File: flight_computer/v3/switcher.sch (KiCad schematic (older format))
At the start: 56 parts, among them J10 Perovskite 3, J11 GaAs Panel, J12 GaAs Temperature, J13 Perovskite 1, J14 Perovskite 2, U15 74HC237, U2 CD4518BM96, U4 74HC237, U42 ADG839YKSZ-REEL7, U43 ADG839YKSZ-REEL7, U44 ADG839YKSZ-REEL7, U45 ADG839YKSZ-REEL7, U46 ADG839YKSZ-REEL7, U47 ADG839YKSZ-REEL7, U48 ADG839YKSZ-REEL7, U49 ADG839YKSZ-REEL7, U5 74HC237, U50 ADG839YKSZ-REEL7, U51 ADG839YKSZ-REEL7, U52 ADG839YKSZ-REEL7, U53 ADG839YKSZ-REEL7, U54 ADG839YKSZ-REEL7, U55 ADG839YKSZ-REEL7, U56 ADG839YKSZ-REEL7, U57 ADG839YKSZ-REEL7, U58 ADG839YKSZ-REEL7, U59 ADG839YKSZ-REEL7, U6 4012

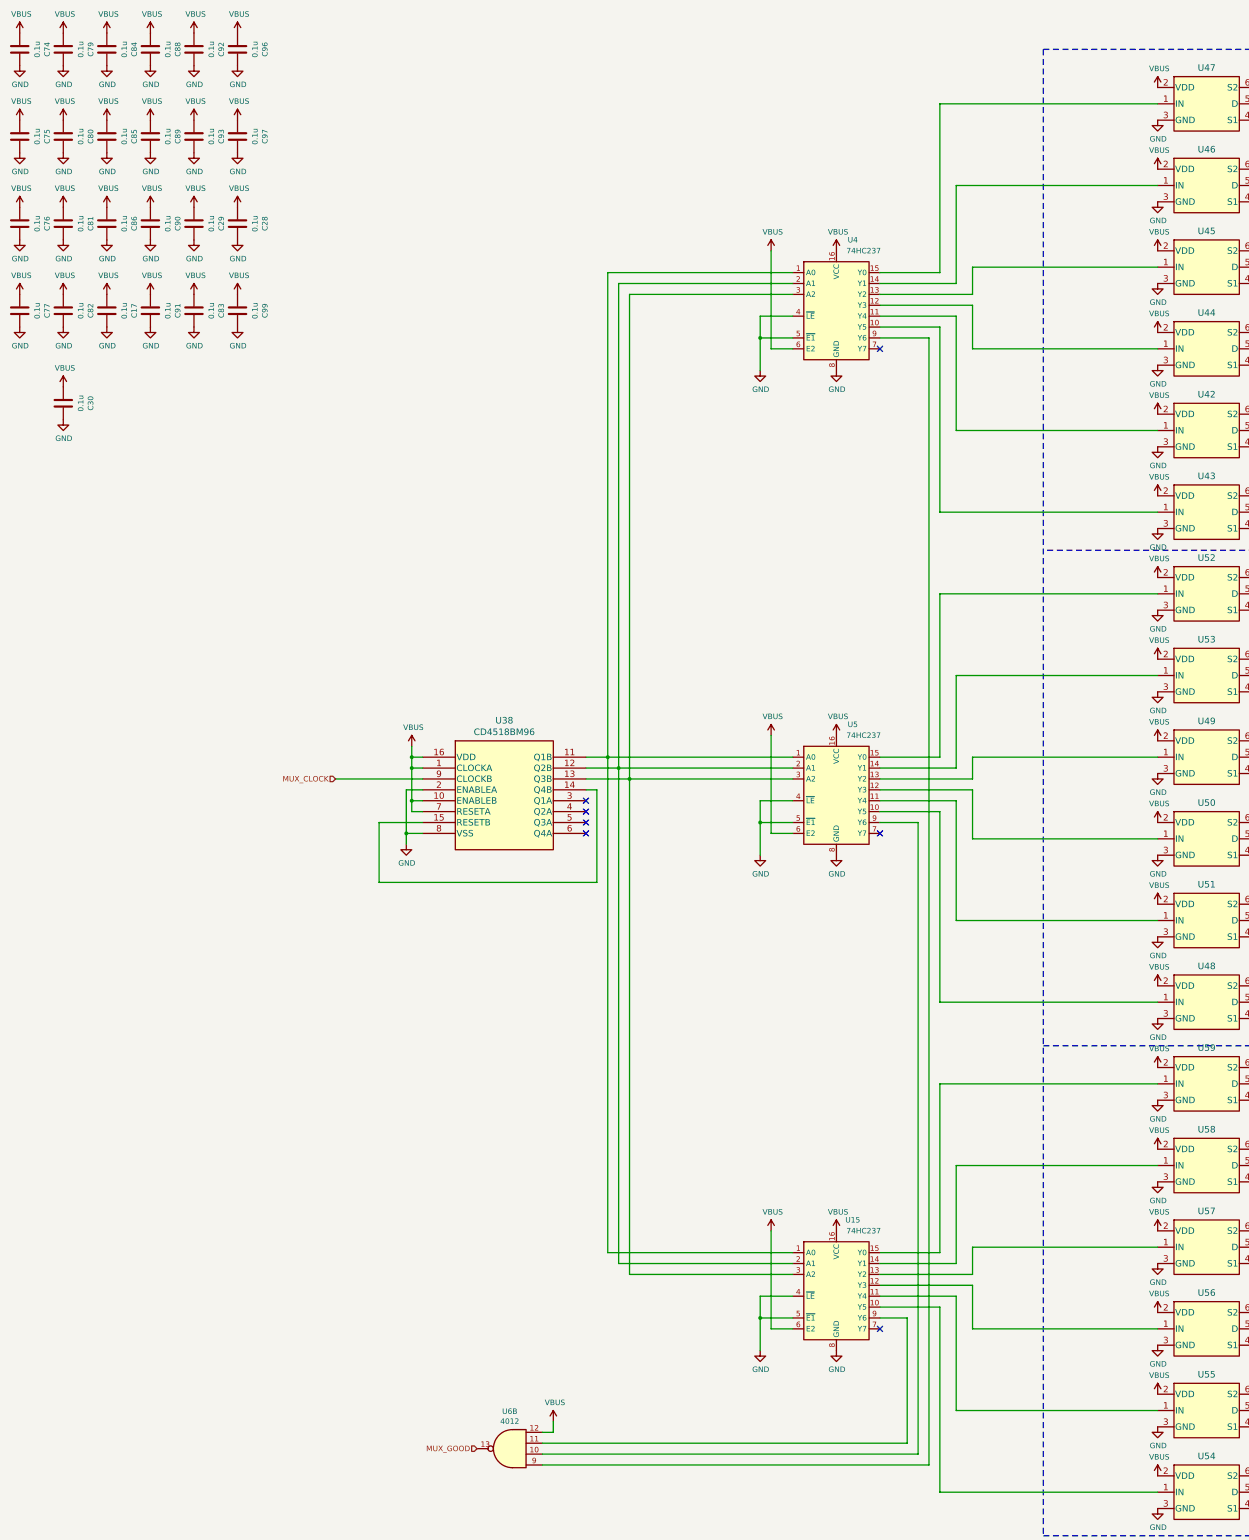
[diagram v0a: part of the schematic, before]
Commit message: Updating based on harnesses
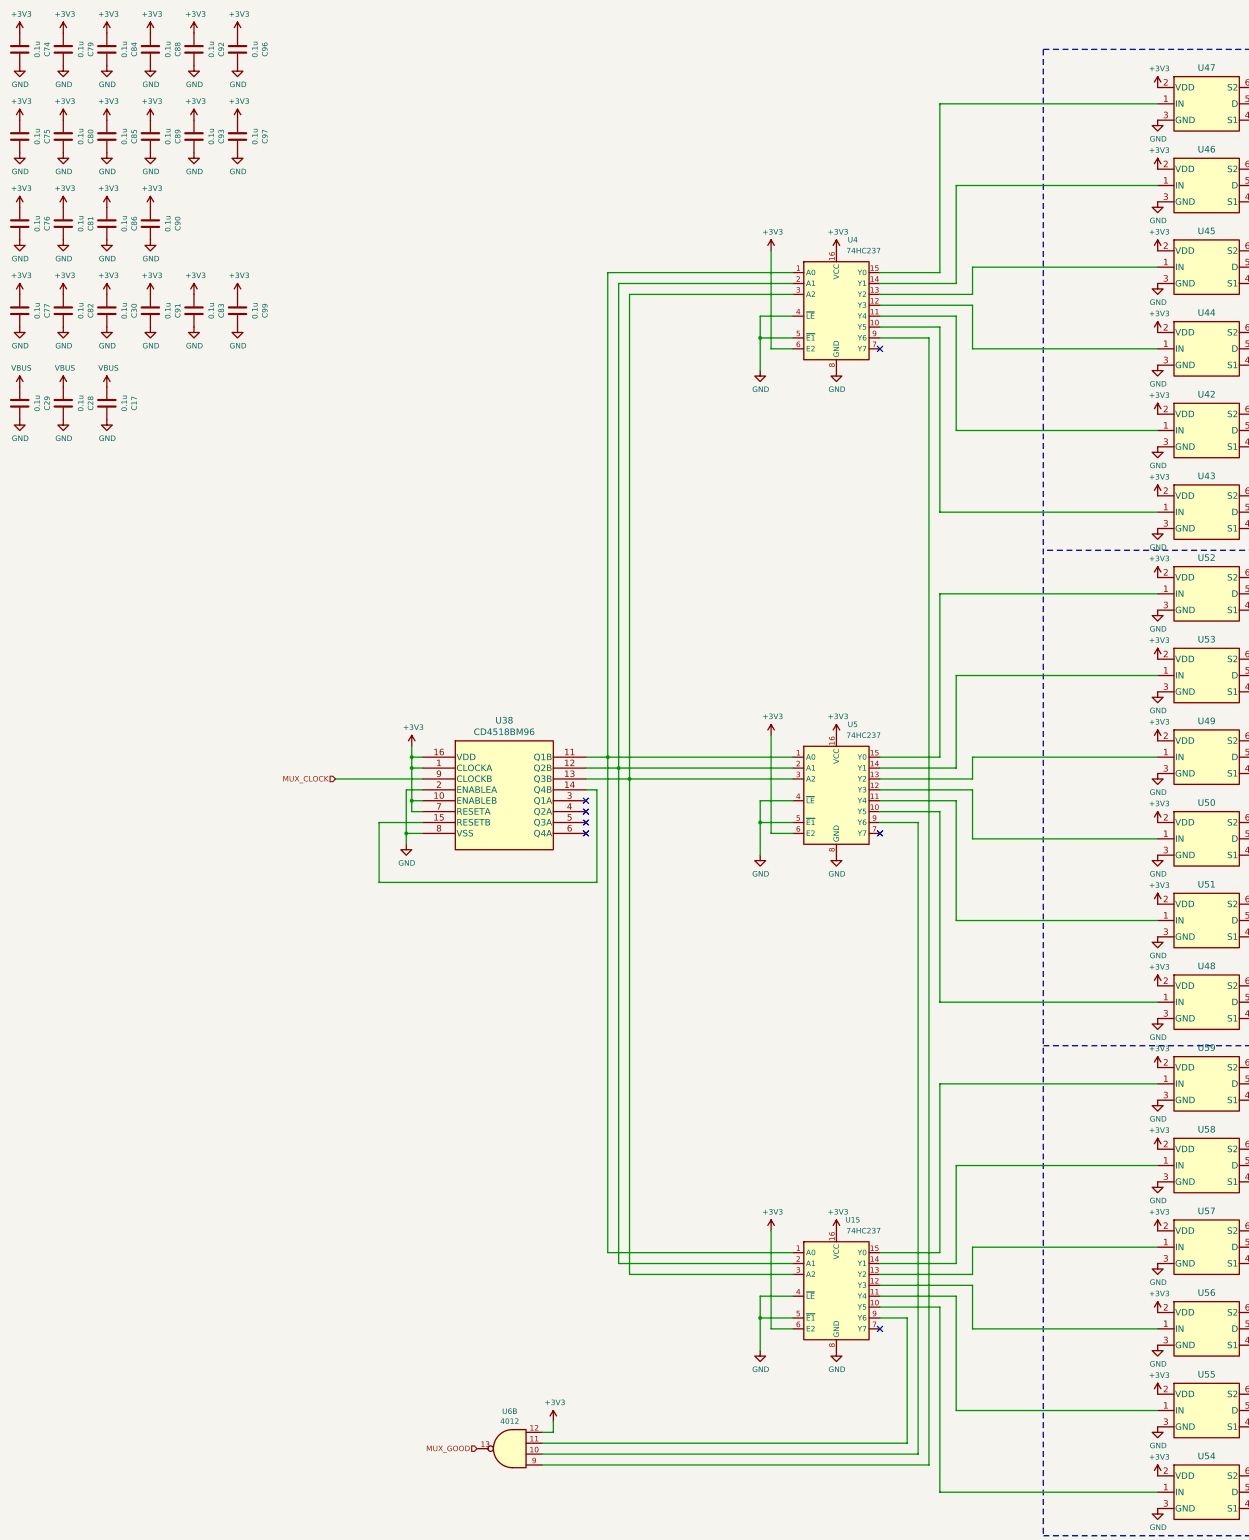
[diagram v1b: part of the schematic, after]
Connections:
- net VBUS: no longer C10.1, C14.1, C16.1, C18.1, C20.1, C25.1, C30.1, C4.1, C6.1, C75.1, C76.1, C8.1, C80.1, C81.1, C83.1, C85.1, C86.1, C89.1, C90.1, C93.1, C97.1, C99.1, U15.16 (VCC), U15.6 (E2), U2.1 (CLOCKA), U2.10 (ENABLEB), U2.16 (VDD), U2.7 (RESETA), U4.16 (VCC), U4.6 (E2), U42.2 (VDD), U43.2 (VDD), U44.2 (VDD), U45.2 (VDD), U46.2 (VDD), U47.2 (VDD), U48.2 (VDD), U49.2 (VDD), U5.16 (VCC), U5.6 (E2), U50.2 (VDD), U51.2 (VDD), U52.2 (VDD), U53.2 (VDD), U54.2 (VDD), U55.2 (VDD), U56.2 (VDD), U57.2 (VDD), U58.2 (VDD), U59.2 (VDD), U6.12
- new net +3V3: C10.1, C14.1, C16.1, C18.1, C20.1, C25.1, C30.1, C4.1, C6.1, C75.1, C76.1, C8.1, C80.1, C81.1, C83.1, C85.1, C86.1, C89.1, C90.1, C93.1, C97.1, C99.1, U15.16 (VCC), U15.6 (E2), U2.1 (CLOCKA), U2.10 (ENABLEB), U2.16 (VDD), U2.7 (RESETA), U4.16 (VCC), U4.6 (E2), U42.2 (VDD), U43.2 (VDD), U44.2 (VDD), U45.2 (VDD), U46.2 (VDD), U47.2 (VDD), U48.2 (VDD), U49.2 (VDD), U5.16 (VCC), U5.6 (E2), U50.2 (VDD), U51.2 (VDD), U52.2 (VDD), U53.2 (VDD), U54.2 (VDD), U55.2 (VDD), U56.2 (VDD), U57.2 (VDD), U58.2 (VDD), U59.2 (VDD), U6.12
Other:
- moved on the sheet: C17, C28, C29, C30

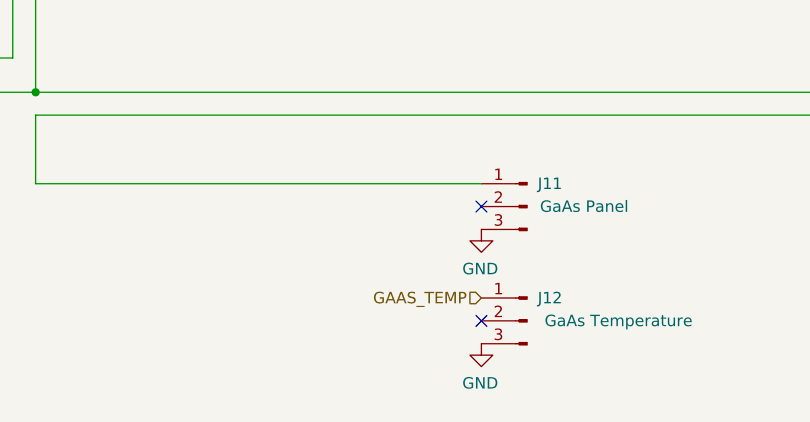
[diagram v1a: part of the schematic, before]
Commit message: Integrating flight computer
- EPS commands tested and working
- Updated v3, fixing connector polarity
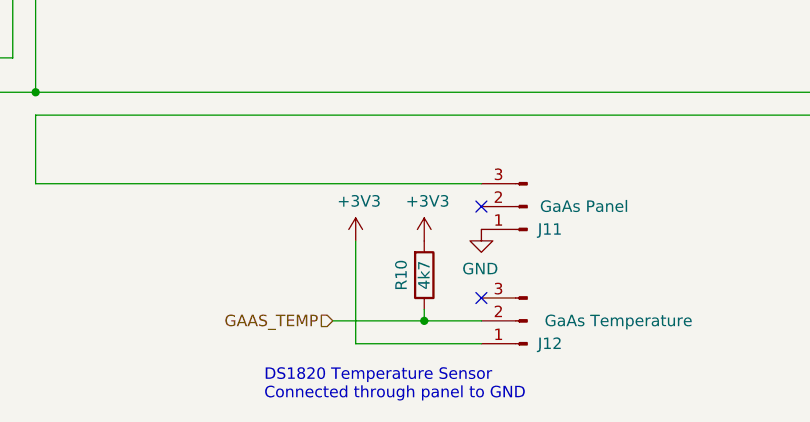
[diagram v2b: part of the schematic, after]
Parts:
- added R10: 4k7, Resistor_SMD:R_0603_1608Metric, symbol Device:R
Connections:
- net +3V3: now also J12.1 (Pin_1), R10.2
- net GAAS_POS: now also J11.3 (Pin_3); no longer J11.1 (Pin_1)
- net GAAS_TEMP: now also J12.2 (Pin_2), R10.1; no longer J12.1 (Pin_1)
- net GND: now also J11.1 (Pin_1); no longer J11.3 (Pin_3), J12.3 (Pin_3)
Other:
- note added: "DS1820 Temperature Sensor\nConnected through panel to GND"
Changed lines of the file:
@@
 F 3 "~" H 16450 14900 50  0001 C CNN
 	1    16450 14900
-	-1   0    0    -1
+	-1   0    0    1
 $EndComp
 NoConn ~ 16250 14900
@@
 F 3 "~" H 16450 15400 50  0001 C CNN
 	1    16450 15400
-	-1   0    0    -1
-$EndComp
-$Comp
-L power:GND #PWR?
-U 1 1 6543CC99
-P 16250 15500
-AR Path="/64A4749F/6543CC99" Ref="#PWR?"  Part="1"
-AR Path="/64A6B33A/6543CC99" Ref="#PWR?"  Part="1"
-AR Path="/64D823E8/6543CC99" Ref="#PWR?"  Part="1"
-AR Path="/64FA0890/6543CC99" Ref="#PWR?"  Part="1"
-AR Path="/64D827F9/6543CC99" Ref="#PWR0314"  Part="1"
-F 0 "#PWR0314" H 16250 15250 50  0001 C CNN
-F 1 "GND" H 16255 15327 50  0000 C CNN
-F 2 "" H 16250 15500 50  0001 C CNN
-F 3 "" H 16250 15500 50  0001 C CNN
-	1    16250 15500
-	-1   0    0    -1
-$EndComp
-NoConn ~ 16250 15400
+	-1   0    0    1
+$EndComp
 Wire Wire Line
 	12300 1500 16300 1500
@@
 Wire Wire Line
 	17000 11400 17300 11400
-Text HLabel 16250 15300 0    50   Input ~ 0
+Text HLabel 15600 15400 0    50   Input ~ 0
 GAAS_TEMP
 $Comp
@@
 	1    0    0    -1
 $EndComp
+NoConn ~ 16250 15300
+$Comp
+L Device:R R?
+U 1 1 64FAD85E
+P 16000 15200
+AR Path="/6313FC31/64FAD85E" Ref="R?"  Part="1"
+AR Path="/64FAD85E" Ref="R?"  Part="1"
+AR Path="/635FE71D/64FAD85E" Ref="R?"  Part="1"
+AR Path="/63D1F518/64FAD85E" Ref="R?"  Part="1"
+AR Path="/63D21EEE/64FAD85E" Ref="R?"  Part="1"
+AR Path="/64AE160A/64FAD85E" Ref="R?"  Part="1"
+AR Path="/64D827F9/64FAD85E" Ref="R10"  Part="1"
+F 0 "R10" V 15900 15200 50  0000 C CNN
+F 1 "4k7" V 16000 15200 50  0000 C CNN
+F 2 "Resistor_SMD:R_0603_1608Metric" V 15930 15200 50  0001 C CNN
+F 3 "~" H 16000 15200 50  0001 C CNN
+	1    16000 15200
+	1    0    0    1
+$EndComp
+$Comp
+L power:+3V3 #PWR?
+U 1 1 64FAD864
+P 16000 15050
+AR Path="/64FAD864" Ref="#PWR?"  Part="1"
+AR Path="/63D1F518/64FAD864" Ref="#PWR?"  Part="1"
+AR Path="/63D21EEE/64FAD864" Ref="#PWR?"  Part="1"
+AR Path="/64AE160A/64FAD864" Ref="#PWR?"  Part="1"
+AR Path="/64D827F9/64FAD864" Ref="#PWR0132"  Part="1"
+F 0 "#PWR0132" H 16000 14900 50  0001 C CNN
+F 1 "+3V3" H 16015 15223 50  0000 C CNN
+F 2 "" H 16000 15050 50  0001 C CNN
+F 3 "" H 16000 15050 50  0001 C CNN
+	1    16000 15050
+	1    0    0    -1
+$EndComp
+Wire Wire Line
+	16000 15350 16000 15400
+Connection ~ 16000 15400
+Wire Wire Line
+	16000 15400 16250 15400
+$Comp
+L power:+3V3 #PWR?
+U 1 1 64FF6664
+P 15700 15050
+AR Path="/64FF6664" Ref="#PWR?"  Part="1"
+AR Path="/63D1F518/64FF6664" Ref="#PWR?"  Part="1"
+AR Path="/63D21EEE/64FF6664" Ref="#PWR?"  Part="1"
+AR Path="/64AE160A/64FF6664" Ref="#PWR?"  Part="1"
+AR Path="/64D827F9/64FF6664" Ref="#PWR0133"  Part="1"
+F 0 "#PWR0133" H 15700 14900 50  0001 C CNN
+F 1 "+3V3" H 15715 15223 50  0000 C CNN
+F 2 "" H 15700 15050 50  0001 C CNN
+F 3 "" H 15700 15050 50  0001 C CNN
+	1    15700 15050
+	1    0    0    -1
+$EndComp
+Wire Wire Line
+	15700 15050 15700 15500
+Wire Wire Line
+	15700 15500 16250 15500
+Wire Wire Line
+	15600 15400 16000 15400
+Text Notes 15300 15750 0    50   ~ 0
+DS1820 Temperature Sensor\nConnected through panel to GND
 $EndSCHEMATC

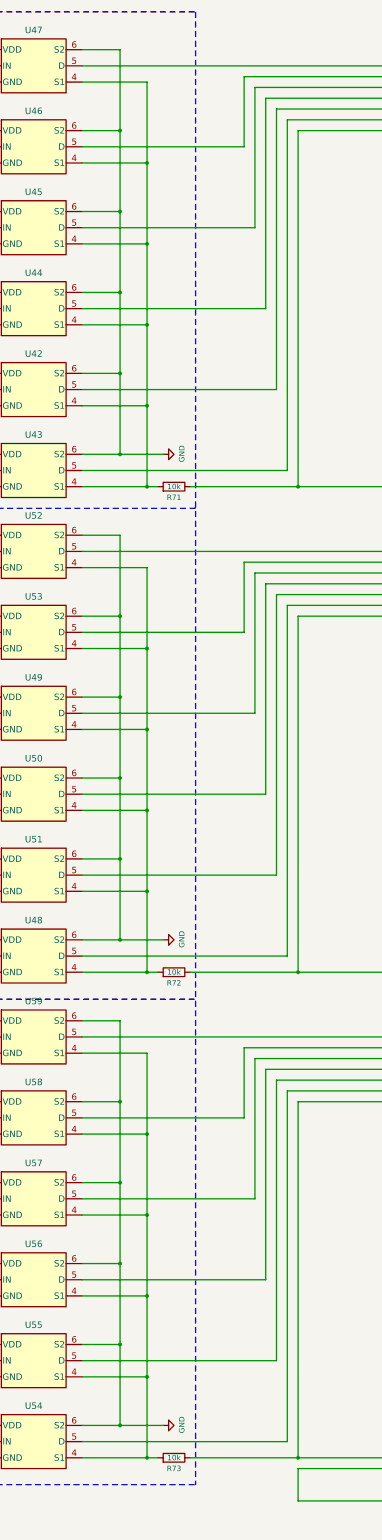
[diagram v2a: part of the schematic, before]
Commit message: Update hardware
- Add separate discharge resistance paths to flight computer
- Update footprint for payload holder
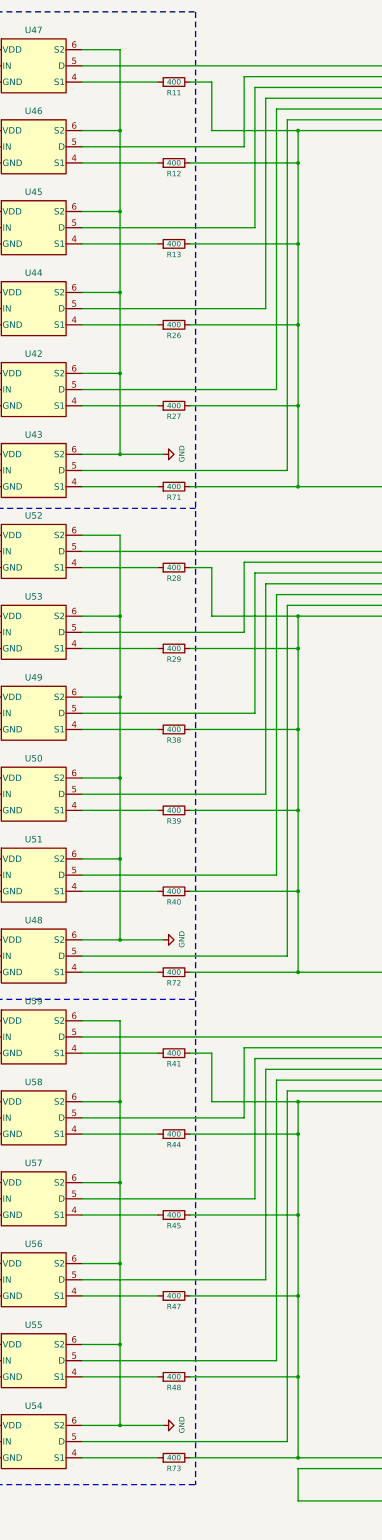
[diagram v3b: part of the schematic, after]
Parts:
- added R11, R12, R13, R26, R27, R28, R29, R38, R39, R40, R41, R44, R45, R47, R48: 400, Resistor_SMD:R_0603_1608Metric, symbol Device:R
- R71, R72, R73: value 10k -> 400
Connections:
- net P1_CP: now also R11.1, R12.1, R13.1, R26.1, R27.1
- net P2_CP: now also R28.1, R29.1, R38.1, R39.1, R40.1
- net P3_CP: now also R41.1, R44.1, R45.1, R47.1, R48.1
- new net: R11.2, U47.4 (S1)
- new net: R26.2, U44.4 (S1)
- new net: R13.2, U45.4 (S1)
- new net: R71.2, U43.4 (S1)
- new net: R12.2, U46.4 (S1)
- new net: R27.2, U42.4 (S1)
- new net: R40.2, U51.4 (S1)
- new net: R39.2, U50.4 (S1)
- new net: R38.2, U49.4 (S1)
- new net: R29.2, U53.4 (S1)
- new net: R28.2, U52.4 (S1)
- new net: R72.2, U48.4 (S1)
- new net: R41.2, U59.4 (S1)
- new net: R47.2, U56.4 (S1)
- new net: R48.2, U55.4 (S1)
- new net: R73.2, U54.4 (S1)
- new net: R44.2, U58.4 (S1)
- new net: R45.2, U57.4 (S1)
